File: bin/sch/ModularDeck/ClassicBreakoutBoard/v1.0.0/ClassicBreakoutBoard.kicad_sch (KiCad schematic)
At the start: 2 parts

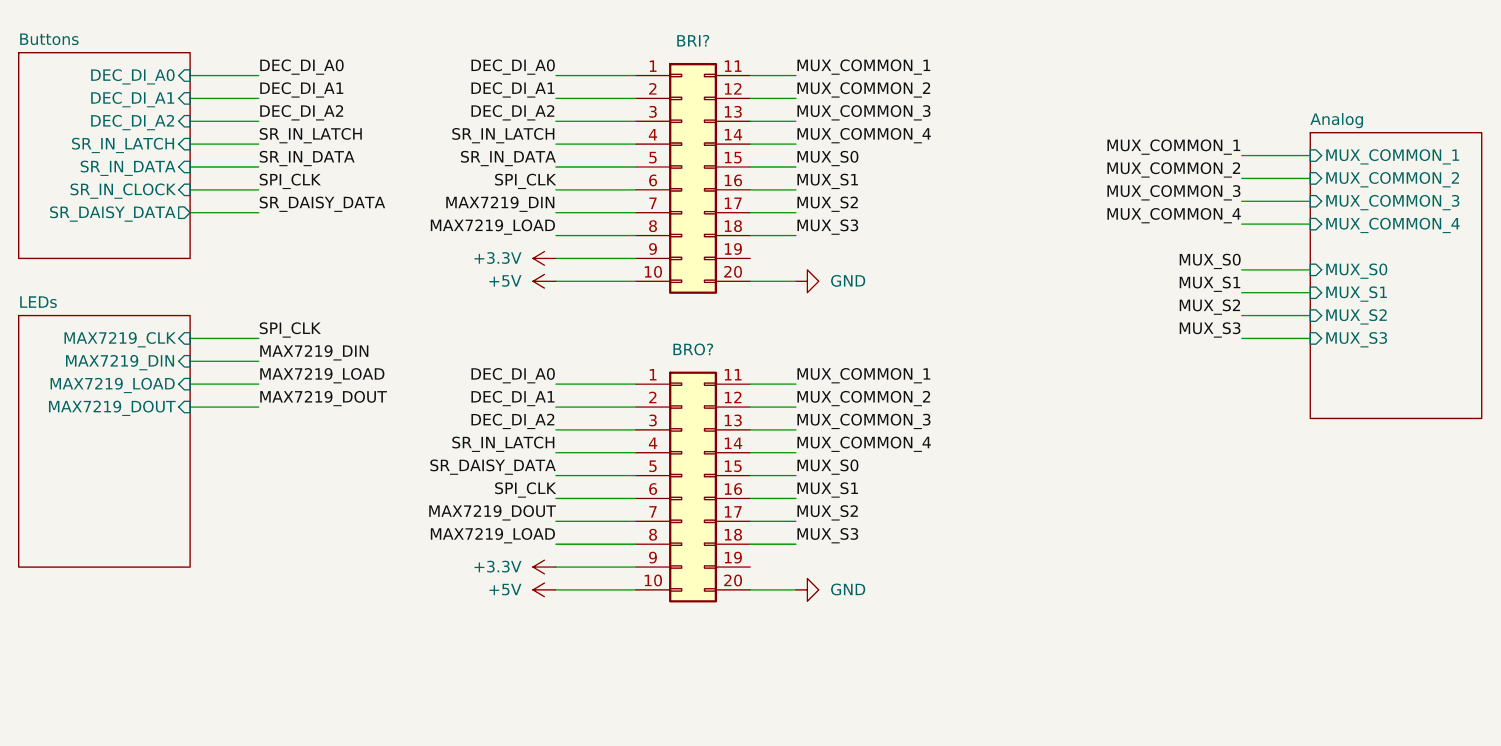
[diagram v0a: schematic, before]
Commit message: Finalised schematics for ModularDeck v1.0.0 (but probably really 0.0.1
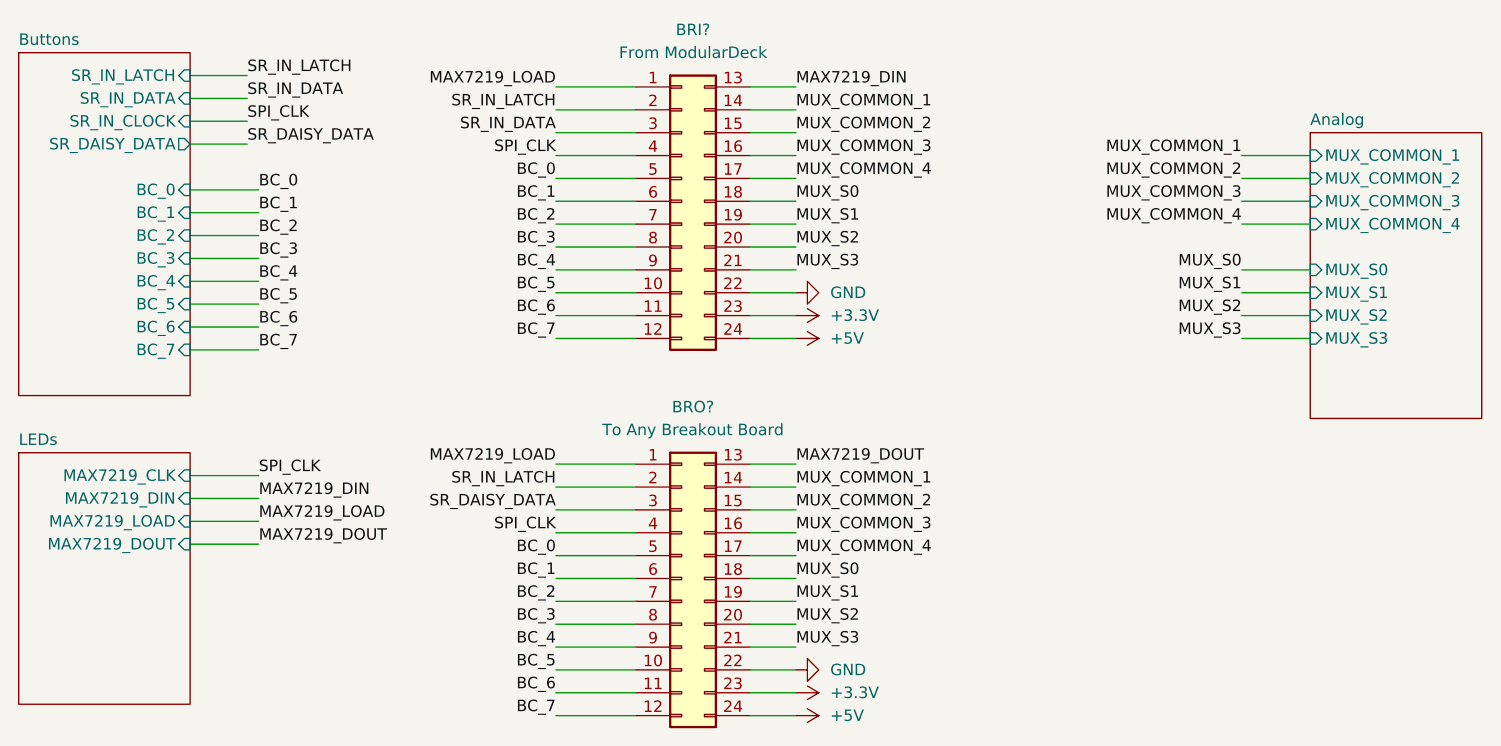
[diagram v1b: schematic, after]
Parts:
- removed BRI?, BRO?: Conn_02x10_Top_Bottom, symbol Connector_Generic:Conn_02x10_Top_Bottom
- added BRI?, BRO?: Conn_02x12_Top_Bottom, symbol Connector_Generic:Conn_02x12_Top_Bottom
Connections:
- net +3.3V: now also BRI?.23 (Pin_23), BRO?.23 (Pin_23)
- net +5V: now also BRI?.24 (Pin_24), BRO?.24 (Pin_24)
- net GND: now also BRI?.22 (Pin_22), BRO?.22 (Pin_22)
- net MAX7219_DIN: now also BRI?.13 (Pin_13)
- net MAX7219_DOUT: now also BRO?.13 (Pin_13)
- net MAX7219_LOAD: now also BRI?.1 (Pin_1), BRO?.1 (Pin_1)
- net MUX_COMMON_1: now also BRI?.14 (Pin_14), BRO?.14 (Pin_14)
- net MUX_COMMON_2: now also BRI?.15 (Pin_15), BRO?.15 (Pin_15)
- net MUX_COMMON_3: now also BRI?.16 (Pin_16), BRO?.16 (Pin_16)
- net MUX_COMMON_4: now also BRI?.17 (Pin_17), BRO?.17 (Pin_17)
- net MUX_S0: now also BRI?.18 (Pin_18), BRO?.18 (Pin_18)
- net MUX_S1: now also BRI?.19 (Pin_19), BRO?.19 (Pin_19)
- net MUX_S2: now also BRI?.20 (Pin_20), BRO?.20 (Pin_20)
- net MUX_S3: now also BRI?.21 (Pin_21), BRO?.21 (Pin_21)
- net SPI_CLK: now also BRI?.4 (Pin_4), BRO?.4 (Pin_4)
- net SR_DAISY_DATA: now also BRO?.3 (Pin_3)
- net SR_IN_DATA: now also BRI?.3 (Pin_3)
- net SR_IN_LATCH: now also BRI?.2 (Pin_2), BRO?.2 (Pin_2)
- new net BC_0: BRI?.5 (Pin_5), BRO?.5 (Pin_5)
- new net BC_1: BRI?.6 (Pin_6), BRO?.6 (Pin_6)
- new net BC_2: BRI?.7 (Pin_7), BRO?.7 (Pin_7)
- new net BC_3: BRI?.8 (Pin_8), BRO?.8 (Pin_8)
- new net BC_4: BRI?.9 (Pin_9), BRO?.9 (Pin_9)
- new net BC_5: BRI?.10 (Pin_10), BRO?.10 (Pin_10)
- new net BC_6: BRI?.11 (Pin_11), BRO?.11 (Pin_11)
- new net BC_7: BRI?.12 (Pin_12), BRO?.12 (Pin_12)
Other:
- sheet Buttons ports: added BC_0, BC_1, BC_2, BC_3, BC_4, BC_5, BC_6, BC_7; removed DEC_DI_A0, DEC_DI_A1, DEC_DI_A2
